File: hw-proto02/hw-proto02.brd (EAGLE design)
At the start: 54.3 x 62.2 mm, 23 parts, among them IC3 MCP2562T, IC5 IR4427S, J1 000, J2 000, Q1 PMOS, Q2 PMOS

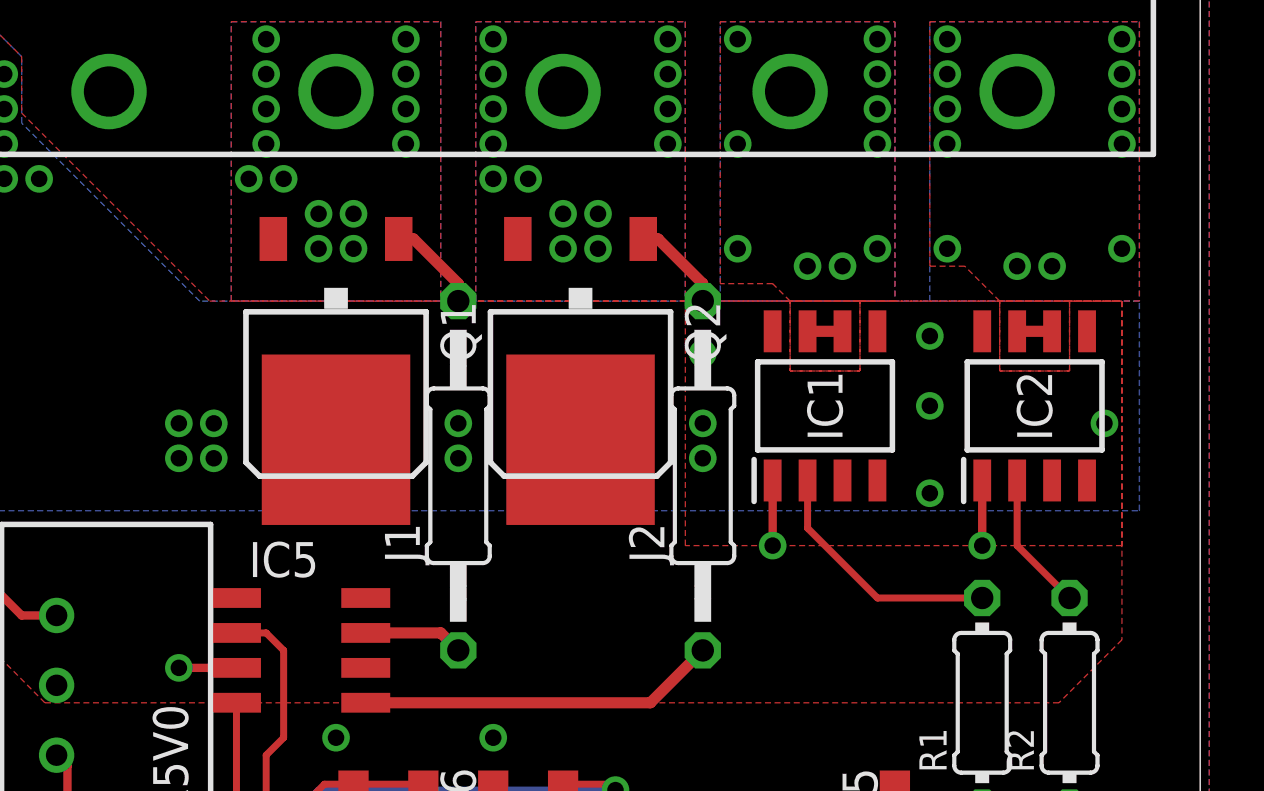
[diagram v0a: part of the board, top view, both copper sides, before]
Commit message: changed to power-so8 fets
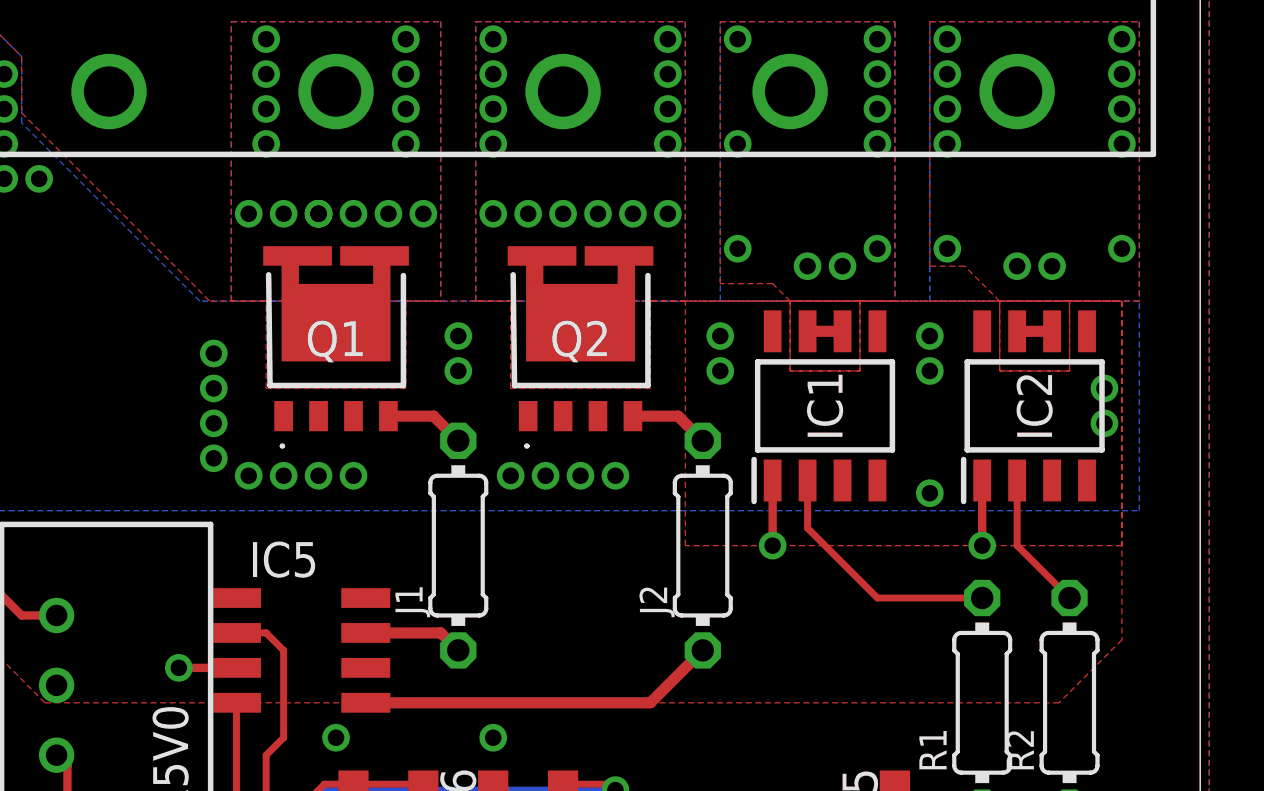
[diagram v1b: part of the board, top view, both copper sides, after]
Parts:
- J1, J2: device rcl:0207/12 -> rcl:0204/7
- Q1, Q2: value PMOS -> SQJ147ELP-T1_GE3; device transistor-mosfet-specialpkg:D-PAK_TO252AA -> transistor-vishay-pchan-pso8:SQJ147ELPT1_GE3
- moved J1 2.54 mm to (27.3, 50.8)
- moved J2 2.54 mm to (36.2, 50.8)
- moved Q1 1.27 mm to (22.9, 58.4), turned to 0 degrees
- moved Q2 1.27 mm to (31.8, 58.4), turned to 0 degrees
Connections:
- net +12V: now also Q1.1, Q1.2, Q1.3, Q2.1, Q2.2, Q2.3; no longer Q1.4, Q2.4
- net N$5: now also Q1.4; no longer Q1.1
- net N$6: now also Q2.4; no longer Q2.1
- net SW1: now also Q1.5, Q1.6, Q1.7, Q1.8, Q1.9; no longer Q1.3
- net SW2: now also Q2.5, Q2.6, Q2.7, Q2.8, Q2.9; no longer Q2.3
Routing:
- net SW2: track 0.00 -> 5.31 mm
- net SW1: track 0.00 -> 1.90 mm, vias 14 -> 15
- net N$6: track 3.47 -> 2.91 mm
- net N$5: track 3.47 -> 2.91 mm
- net +12V: vias 34 -> 42

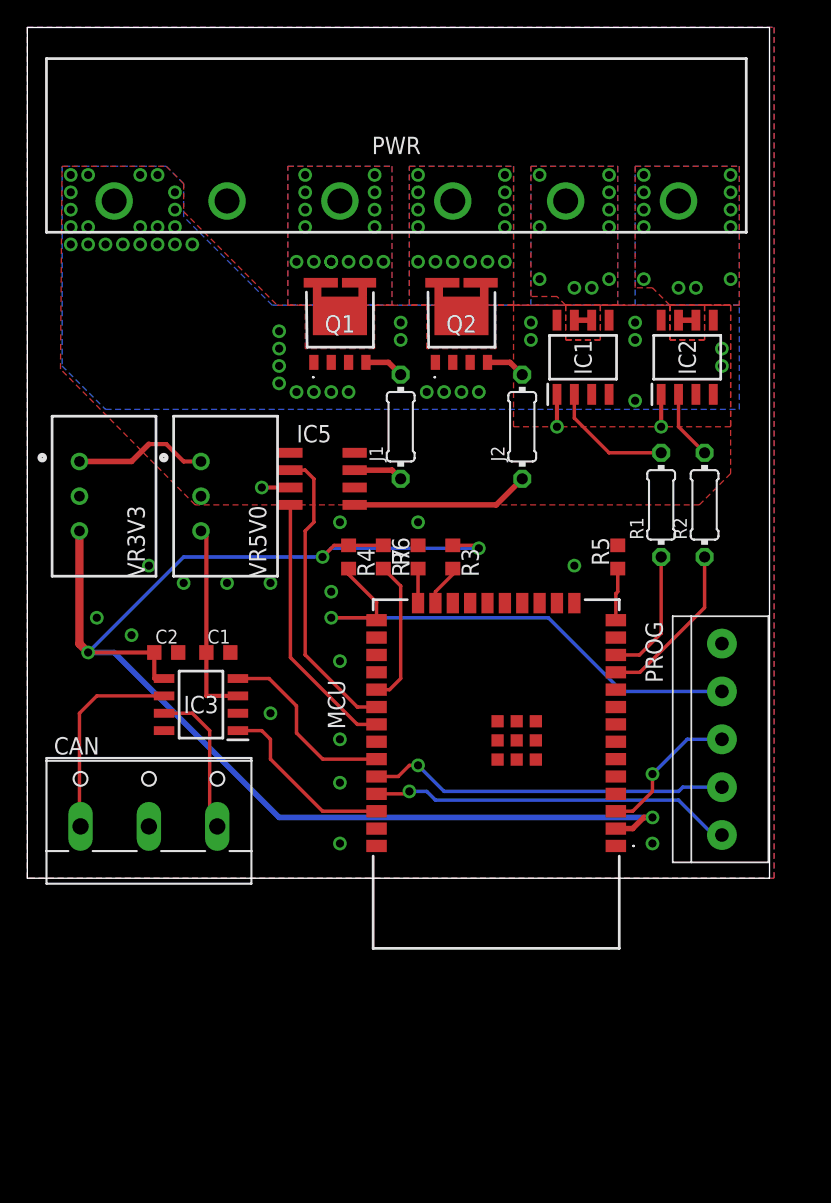
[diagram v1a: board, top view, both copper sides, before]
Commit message: made the +12v connection more chonky
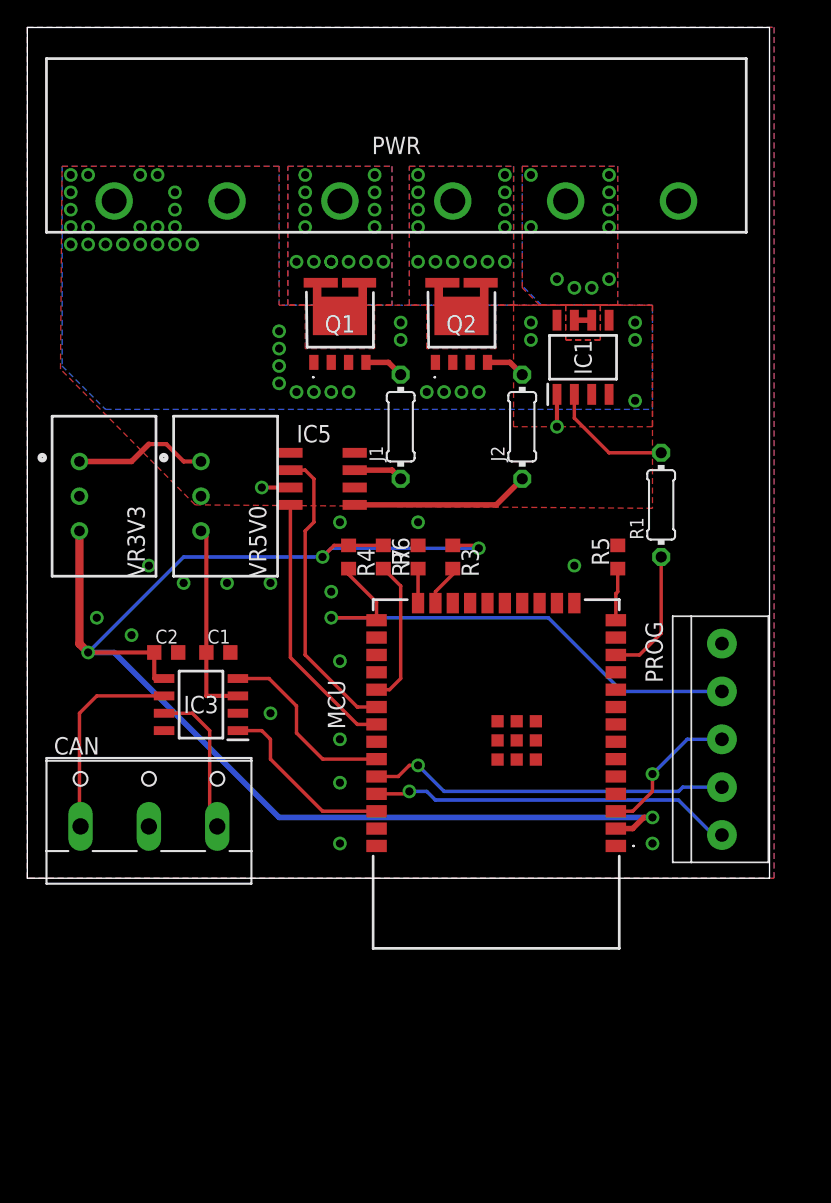
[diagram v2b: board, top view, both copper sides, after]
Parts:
- removed IC2: (no value), VN5E160MSTR-E:SOIC127P600X175-8N
- removed R2: 10K0, rcl:0204/7
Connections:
- removed net N$8: IC2.2, R2.2
- removed net SW4: IC2.6, IC2.7, PWR.6
- net +12V: now also PWR.2; no longer IC2.5, IC2.8
- net CTL4: no longer R2.1
- net GND: now also PWR.6; no longer IC2.1, PWR.2
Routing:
- net CTL4: track 12.2 -> 0.00 mm
- net N$8: track 5.06 -> 0.00 mm
- net GND: track 6.83 -> 4.46 mm, vias 19 -> 18
- net SW4: track 1.27 -> 0.00 mm, vias 12 -> 0
- net +12V: vias 42 -> 40
- removed copper zone on layer 1, net SW4
- removed copper zone on layer 16, net SW4
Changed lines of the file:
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@@
 <attribute name="MOUSER_PRICE-STOCK" value="https://www.mouser.co.uk/ProductDetail/STMicroelectronics/VN5E160MSTR-E?qs=WSSg0AwdCh77XxtxsYEeyw%3D%3D" x="40.64" y="55.88" size="1.778" layer="27" rot="R90" display="off"/>
-</element>
-<element name="IC2" library="VN5E160MSTR-E" package="SOIC127P600X175-8N" value="" x="48.26" y="55.88" rot="R90">
-<attribute name="MANUFACTURER_PART_NUMBER" value="VN5E160MSTR-E" x="48.26" y="55.88" size="1.778" layer="27" rot="R90" display="off"/>
-<attribute name="DESCRIPTION" value="Gate Drivers SNGL CH HI-SIDE DRVR W/ANALOG CRRNT SNSE" x="48.26" y="55.88" size="1.778" layer="27" rot="R90" display="off"/>
-<attribute name="MANUFACTURER_NAME" value="STMicroelectronics" x="48.26" y="55.88" size="1.778" layer="27" rot="R90" display="off"/>
-<attribute name="MOUSER_PART_NUMBER" value="511-VN5E160MSTR-E" x="48.26" y="55.88" size="1.778" layer="27" rot="R90" display="off"/>
-<attribute name="HEIGHT" value="1.75mm" x="48.26" y="55.88" size="1.778" layer="27" rot="R90" display="off"/>
-<attribute name="MOUSER_PRICE-STOCK" value="https://www.mouser.co.uk/ProductDetail/STMicroelectronics/VN5E160MSTR-E?qs=WSSg0AwdCh77XxtxsYEeyw%3D%3D" x="48.26" y="55.88" size="1.778" layer="27" rot="R90" display="off"/>
 </element>
 <element name="IC3" library="MCP2562T-H_SN" package="SOIC127P600X175-8N" value="MCP2562T" x="12.7" y="30.48" rot="R180">
@@
 <element name="J2" library="rcl" package="0204/7" value="000" x="36.195" y="50.8" rot="R90"/>
 <element name="R1" library="rcl" package="0204/7" value="10K0" x="46.355" y="45.085" rot="R90"/>
-<element name="R2" library="rcl" package="0204/7" value="10K0" x="49.53" y="45.085" rot="R90"/>
 <element name="C1" library="rcl" package="C0603K" value="100n" x="13.97" y="34.29"/>
 <element name="C2" library="rcl" package="C0603K" value="100n" x="10.16" y="34.29"/>
@@
 <vertex x="39.37" y="57.15"/>
 <vertex x="39.37" y="59.69"/>
-<vertex x="38.735" y="60.325"/>
-<vertex x="36.83" y="60.325"/>
-<vertex x="36.83" y="69.85"/>
+<vertex x="37.465" y="59.69"/>
+<vertex x="36.195" y="60.96"/>
+<vertex x="36.195" y="69.85"/>
 <vertex x="43.18" y="69.85"/>
 <vertex x="43.18" y="59.69"/>
@@
 </polygon>
 <polygon width="0.4064" layer="16" spacing="0.3048" isolate="0.254" thermals="no" rank="2">
-<vertex x="36.83" y="69.85"/>
+<vertex x="36.195" y="69.85"/>
 <vertex x="43.18" y="69.85"/>
 <vertex x="43.18" y="59.69"/>
-<vertex x="36.83" y="59.69"/>
-</polygon>
-<via x="37.465" y="69.215" extent="1-16" drill="0.6"/>
+<vertex x="37.614903125" y="59.69"/>
+<vertex x="36.195" y="61.109903125"/>
+</polygon>
+<via x="36.83" y="69.215" extent="1-16" drill="0.6"/>
 <via x="42.545" y="69.215" extent="1-16" drill="0.6"/>
 <via x="42.545" y="67.945" extent="1-16" drill="0.6"/>
 <via x="42.545" y="66.675" extent="1-16" drill="0.6"/>
 <via x="42.545" y="65.405" extent="1-16" drill="0.6"/>
-<via x="37.465" y="65.405" extent="1-16" drill="0.6"/>
-<via x="37.465" y="61.595" extent="1-16" drill="0.6"/>
+<via x="36.83" y="65.405" extent="1-16" drill="0.6"/>
+<via x="38.735" y="61.595" extent="1-16" drill="0.6"/>
 <via x="42.545" y="61.595" extent="1-16" drill="0.6"/>
 <via x="40.005" y="60.96" extent="1-16" drill="0.6"/>
 <via x="41.275" y="60.96" extent="1-16" drill="0.6"/>
-</signal>
-<signal name="SW4">
-<contactref element="IC2" pad="6"/>
-<contactref element="IC2" pad="7"/>
-<wire x1="47.625" y1="58.592" x2="48.895" y2="58.592" width="0.4064" layer="1"/>
-<contactref element="PWR" pad="6"/>
-<polygon width="0.4064" layer="1" spacing="0.3048" isolate="0.254" thermals="no" rank="2">
-<vertex x="46.99" y="59.69"/>
-<vertex x="46.99" y="57.15"/>
-<vertex x="49.53" y="57.15"/>
-<vertex x="49.53" y="59.69"/>
-</polygon>
-<polygon width="0.4064" layer="1" spacing="0.3048" isolate="0.254" rank="2">
-<vertex x="46.99" y="57.15"/>
-<vertex x="46.99" y="59.69"/>
-<vertex x="45.72" y="60.96"/>
-<vertex x="44.45" y="60.96"/>
-<vertex x="44.45" y="69.85"/>
-<vertex x="52.07" y="69.85"/>
-<vertex x="52.07" y="59.69"/>
-<vertex x="49.53" y="59.69"/>
-<vertex x="49.53" y="57.15"/>
-</polygon>
-<polygon width="0.4064" layer="16" spacing="0.3048" isolate="0.254" thermals="no" rank="2">
-<vertex x="44.45" y="69.85"/>
-<vertex x="52.07" y="69.85"/>
-<vertex x="52.07" y="59.69"/>
-<vertex x="44.45" y="59.69"/>
-</polygon>
-<via x="45.085" y="69.215" extent="1-16" drill="0.6"/>
-<via x="51.435" y="69.215" extent="1-16" drill="0.6"/>
-<via x="51.435" y="67.945" extent="1-16" drill="0.6"/>
-<via x="51.435" y="66.675" extent="1-16" drill="0.6"/>
-<via x="51.435" y="65.405" extent="1-16" drill="0.6"/>
-<via x="45.085" y="65.405" extent="1-16" drill="0.6"/>
-<via x="45.085" y="66.675" extent="1-16" drill="0.6"/>
-<via x="45.085" y="67.945" extent="1-16" drill="0.6"/>
-<via x="45.085" y="61.595" extent="1-16" drill="0.6"/>
-<via x="47.625" y="60.96" extent="1-16" drill="0.6"/>
-<via x="48.895" y="60.96" extent="1-16" drill="0.6"/>
-<via x="51.435" y="61.595" extent="1-16" drill="0.6"/>
 </signal>
 <signal name="GND">
@@
 <contactref element="MCU" pad="1"/>
 <contactref element="MCU" pad="15"/>
-<contactref element="PWR" pad="2"/>
 <contactref element="IC1" pad="1"/>
-<contactref element="IC2" pad="1"/>
 <contactref element="VR3V3" pad="2"/>
 <contactref element="VR5V0" pad="2"/>
@@
 <contactref element="IC5" pad="3"/>
 <via x="38.735" y="50.8" extent="1-16" drill="0.6" shape="octagon"/>
-<via x="46.355" y="50.8" extent="1-16" drill="0.6" shape="octagon"/>
 <wire x1="38.735" y1="53.168" x2="38.735" y2="50.8" width="0.3048" layer="1"/>
-<wire x1="46.355" y1="53.168" x2="46.355" y2="50.8" width="0.3048" layer="1"/>
 <via x="17.145" y="46.355" extent="1-16" drill="0.6" shape="octagon"/>
 <wire x1="19.24" y1="46.355" x2="17.145" y2="46.355" width="0.3048" layer="1"/>
@@
 <via x="5.08" y="36.83" extent="1-16" drill="0.6"/>
 <via x="8.89" y="40.64" extent="1-16" drill="0.6"/>
+<contactref element="PWR" pad="6"/>
 </signal>
 <signal name="SW1">
@@
 <polygon width="0.4064" layer="1" spacing="0.3048" isolate="0.254" rank="4">
 <vertex x="2.54" y="69.85"/>
-<vertex x="10.16" y="69.85"/>
-<vertex x="11.43" y="68.58"/>
-<vertex x="11.43" y="66.52915625"/>
-<vertex x="18.26915625" y="59.69"/>
-<vertex x="51.435" y="59.69"/>
-<vertex x="51.435" y="47.374525"/>
-<vertex x="49.145475" y="45.085"/>
+<vertex x="18.415" y="69.85"/>
+<vertex x="18.415" y="59.69"/>
+<vertex x="45.72" y="59.69"/>
+<vertex x="45.72" y="44.834525"/>
 <vertex x="12.27414375" y="45.085"/>
 <vertex x="2.42370625" y="55.012928125"/>
@@
 <contactref element="IC1" pad="5"/>
 <contactref element="IC1" pad="8"/>
-<contactref element="IC2" pad="5"/>
-<contactref element="IC2" pad="8"/>
 <contactref element="IC5" pad="6"/>
 <polygon width="0.4064" layer="1" spacing="0.3048" isolate="0.254" thermals="no" rank="4">
 <vertex x="35.56" y="59.69"/>
-<vertex x="51.435" y="59.69"/>
-<vertex x="51.435" y="50.8"/>
+<vertex x="45.72" y="59.69"/>
+<vertex x="45.72" y="50.8"/>
 <vertex x="35.56" y="50.8"/>
 </polygon>
@@
 <vertex x="2.54" y="55.245"/>
 <vertex x="5.715" y="52.07"/>
-<vertex x="52.07" y="52.07"/>
-<vertex x="52.07" y="59.69"/>
-<vertex x="17.905753125" y="59.69"/>
-<vertex x="11.43" y="66.165753125"/>
-<vertex x="11.43" y="68.58"/>
-<vertex x="10.16" y="69.85"/>
+<vertex x="45.72" y="52.07"/>
+<vertex x="45.72" y="59.69"/>
+<vertex x="18.415" y="59.69"/>
+<vertex x="18.415" y="69.85"/>
 </polygon>
 <via x="18.415" y="55.245" extent="1-16" drill="0.6"/>
@@
 <via x="44.45" y="52.705" extent="1-16" drill="0.6"/>
 <via x="44.45" y="58.42" extent="1-16" drill="0.6"/>
-<via x="50.8" y="55.245" extent="1-16" drill="0.6"/>
 <via x="3.175" y="64.135" extent="1-16" drill="0.6"/>
 <via x="4.445" y="64.135" extent="1-16" drill="0.6"/>
@@
 <via x="36.83" y="58.42" extent="1-16" drill="0.6"/>
 <via x="36.83" y="57.15" extent="1-16" drill="0.6"/>
-<via x="50.8" y="56.515" extent="1-16" drill="0.6"/>
+<contactref element="PWR" pad="2"/>
 </signal>
 <signal name="+5V">
@@
 </signal>
 <signal name="CTL4">
-<contactref element="R2" pad="1"/>
 <contactref element="MCU" pad="11"/>
-<wire x1="43.04" y1="32.84" x2="44.800128125" y2="32.84" width="0.254" layer="1"/>
-<wire x1="44.800128125" y1="32.84" x2="49.53" y2="37.569871875" width="0.254" layer="1"/>
-<wire x1="49.53" y1="37.569871875" x2="49.53" y2="41.275" width="0.254" layer="1"/>
 </signal>
 <signal name="CTL3">
@@
 <wire x1="42.545" y1="48.895" x2="46.355" y2="48.895" width="0.254" layer="1"/>
 </signal>
-<signal name="N$8">
-<contactref element="R2" pad="2"/>
-<contactref element="IC2" pad="2"/>
-<wire x1="49.53" y1="48.895" x2="47.625" y2="50.8" width="0.254" layer="1"/>
-<wire x1="47.625" y1="50.8" x2="47.625" y2="53.168" width="0.254" layer="1"/>
-</signal>
 <signal name="GPIO15">

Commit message: power layout adjustment, added passives
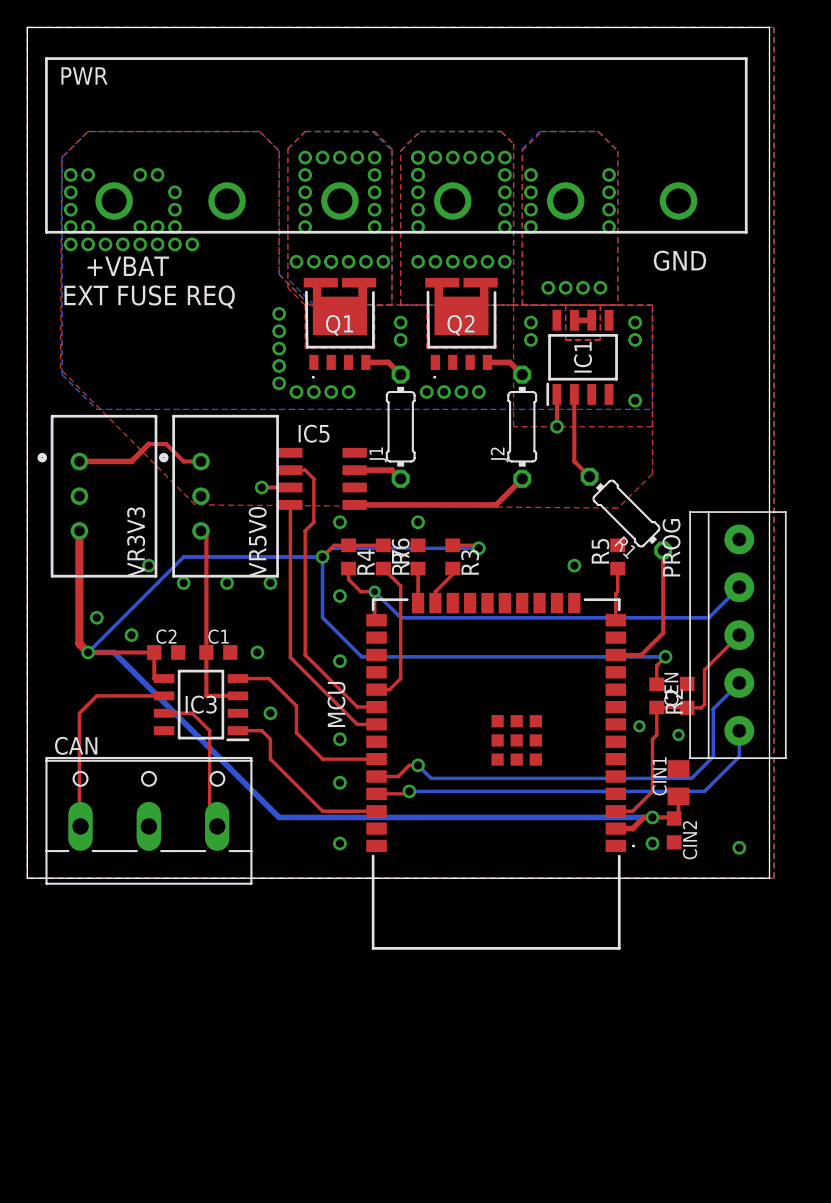
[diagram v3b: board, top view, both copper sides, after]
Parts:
- added CEN: 1u, rcl:C0603K
- added CIN1: 22u, rcl:C0805K
- added CIN2: 100n, rcl:C0603K
- added R2: 10K0, rcl:R0603
- moved PROG 7.73 mm to (52.1, 35.6)
- moved R1 2.62 mm to (43.8, 44.5), turned to 135 degrees
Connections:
- net +3V3: now also CIN1.1, CIN2.1, R2.1
- net EN: now also CEN.1, R2.2
- net GND: now also CEN.2, CIN1.2, CIN2.2
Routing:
- net +3V3: track 104.6 -> 140.9 mm, vias 4 -> 5
- net EN: track 10.7 -> 19.3 mm, vias 1 -> 0
- net RXD0: track 26.5 -> 32.2 mm
- net GPIO0: track 38.9 -> 33.7 mm
- net TXD0: track 26.7 -> 29.5 mm
- net N$7: track 9.14 -> 6.49 mm
- net CTL3: track 9.55 -> 10.2 mm
- net SW3: vias 10 -> 12
- net SW2: vias 14 -> 22
- net SW1: vias 15 -> 20
- net GND: vias 18 -> 22
- net +12V: vias 40 -> 41
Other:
- board text added: "+VBAT EXT FUSE REQ"
- board text added: "GND"
